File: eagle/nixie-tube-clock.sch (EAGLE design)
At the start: 88 parts, among them IC1 HV5622QC, IC2 HV5622QC, IC3 LM555D, IC5 LD117ADT33TR, P1 1 k, Q1 BC817-25SMD, Q2 BC817-25SMD, Q3 BC817-25SMD, Q4 BC817-25SMD, T1 BC547B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

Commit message: Alfa v2 version of schematic
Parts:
- removed R39, R40, R41, R42: 100 k, resistor:R-EU_R1206
- Q1, Q2, Q3, Q4: value BC817-25SMD -> BSS138; device transistor-npn:BC817-25SMD -> transistor-small-signal:BSS123
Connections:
- removed net N$1: Q1.B, R39.1
- removed net N$17: Q3.B, R41.1
- removed net N$2: Q2.B, R40.1
- removed net N$31: Q4.B, R42.1
- net +12V: now also Q1.D, Q2.D; no longer R37.2, R38.2
- net BL: now also Q4.D; no longer Q4.C
- net CLK: now also Q2.S, R37.2; no longer Q2.C, R37.1
- net GND: now also Q3.S, Q4.S, R37.1, R38.1; no longer Q1.E, Q2.E, Q3.E, Q4.E
- net LE: now also Q3.D; no longer Q3.C
- net MOSI: now also Q1.S, R38.2; no longer Q1.C, R38.1
- net N$19: now also Q4.G; no longer R42.2
- net N$23: now also Q1.G; no longer R39.2
- net N$25: now also Q2.G; no longer R40.2
- net N$29: now also Q3.G; no longer R41.2
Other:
- moved on the sheet: R37, R38

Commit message: Beta version of schematic
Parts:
- removed LSP1: SCL, solpad:SE11
- removed LSP2: MISO, solpad:SE11
- removed LSP3: MOSI, solpad:SE11
- removed LSP4: VCC, solpad:SE11
- removed LSP5: RST, solpad:SE11
- removed Q2, Q3: BSS138, transistor-small-signal:BSS123
- removed R32, R33, R34: 470, resistor:R-EU_R1206
- removed U$1: TINY2313, atmel:TINY2313
- removed X4: (no value), con-ptr500:AK300/2
- added +: +, testpad:TPPAD1-17
- added -: -, testpad:TPPAD1-17
- added C8, C9: 22 pF, resistor:C-EUC1206
- added IC4: MEGA8-AI, atmel:MEGA8-AI
- added MISO: MISO, solpad:SE11
- added MOSI: MOSI, solpad:SE11
- added RST: RST, solpad:SE11
- added SCK: SCK, solpad:SE11
- added T7, T8, T9: IRLL014NTRPBF, transistor-fet:IRLL014NTRPBF
- added VCC: VCC, solpad:SE11
- C1: value 47 uF / 16 V -> 100 uF / 16 V
- D1: value GF1 -> 1A 600V
- Q1: value BSS138 -> 8 MHz; device transistor-small-signal:BSS123 -> crystal:CRYSTALHC49S
- R13, R46: value 270 -> 330k
- R16, R17, R19, R20, R22, R23, R25, R26: value 150 -> 270
- R18, R21, R24, R27: value 180 -> 330
- T3, T4, T5: value BST51 -> BSS138; device transistor:-NPN-SOT89-BCE -> transistor-small-signal:BSS123
- renumbered D2 to D1, Q4 to T6
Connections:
- removed net N$135: R34.2, T5.B
- removed net N$136: R32.2, T3.B
- removed net N$137: R33.2, T4.B
- removed net N$24: LED2-B.C
- removed net N$30: LED3-B.C
- removed net N$35: LSP5.MP, U$1.PA2(RESET/DW)
- removed net N$36: LED4-B.C
- removed net N$37: LSP3.MP, U$1.(MOSI/DI/SDA/PCINT5)PB5
- removed net N$42: LED5-B.C
- removed net N$48: LED6-B.C
- removed net N$54: LED7-B.C
- new net N$1: IC4.PC6(/RESET), RST.MP
- new net N$17: IC4.PB4(MISO), MISO.MP
- new net N$2: IC4.PB3(MOSI/OC2), MOSI.MP, T3.G
- new net N$31: C9.1, IC4.PB6(XTAL1/TOSC1), Q1.1
- net +12V: now also +.TP, T3.D, T4.D; no longer Q1.D, Q2.D, X4-1.KL
- net +3V3: now also IC4.AVCC, IC4.VCC@1, IC4.VCC@2, VCC.MP; no longer LSP4.MP, U$1.VCC
- net CLK: now also T4.S; no longer Q2.S
- net E_RX: now also IC4.PD1(TXD); no longer U$1.(TXD)PD1
- net E_TX: now also IC4.PD0(RXD); no longer U$1.(RXD)PD0
- net GND: now also -.TP, C8.2, C9.2, IC4.GND, IC4.GND@1, IC4.GND@2, T5.S, T7.S, T8.S, T9.S; no longer Q3.S, T3.E, T4.E, T5.E, U$1.GND, X4-2.KL
- net LE: now also T5.D; no longer Q3.D
- net LED_B: now also LED2-B.C, LED3-B.C, LED4-B.C, LED5-B.C, LED6-B.C, LED7-B.C, T7.D; no longer T4.C
- net LED_D0: now also IC4.PC0(ADC0), T9.G; no longer R34.1, U$1.(OC0A/PCINT2)PB2
- net LED_D1: now also IC4.PC1(ADC1), T8.G; no longer R32.1, U$1.(OC1A/PCINT3)PB3
- net LED_D2: now also IC4.PC2(ADC2), T7.G; no longer R33.1, U$1.(OC1B/PCINT4)PB4
- net LED_G: now also T8.D; no longer T3.C
- net LED_R: now also T9.D; no longer T5.C
- net MIN_1_0: now also IC2.HVOUT23; no longer IC2.HVOUT22, IC2.HVOUT32
- net MIN_1_1: now also IC2.HVOUT24; no longer IC2.HVOUT23
- net MIN_1_2: now also IC2.HVOUT25; no longer IC2.HVOUT24
- net MIN_1_3: now also IC2.HVOUT26; no longer IC2.HVOUT25
- net MIN_1_4: now also IC2.HVOUT27; no longer IC2.HVOUT26
- net MIN_1_5: now also IC2.HVOUT28; no longer IC2.HVOUT27
- net MIN_1_6: now also IC2.HVOUT29; no longer IC2.HVOUT28
- net MIN_1_7: now also IC2.HVOUT30; no longer IC2.HVOUT29
- net MIN_1_8: now also IC2.HVOUT31; no longer IC2.HVOUT30
- net MIN_1_9: now also IC2.HVOUT32; no longer IC2.HVOUT31
- net MOSI: now also T3.S; no longer Q1.S
- net N$19: now also IC4.PB1(OC1A); no longer U$1.(ICP)PD6
- net N$23: now also C8.1, IC4.PB7(XTAL2/TOSC2), Q1.2; no longer LSP2.MP, Q1.G, U$1.(MISO/DO/PCINT6)PB6
- net N$25: now also IC4.PB5(SCK), SCK.MP, T4.G; no longer LSP1.MP, Q2.G, U$1.(UCSK/SCL/PCINT7)PB7
- net N$29: now also IC4.PB0(ICP), T5.G; no longer Q3.G, U$1.(OC0B/T1)PD5
- net RST: now also IC4.PD2(INT0); no longer U$1.(T0)PD4
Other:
- moved on the sheet: R37, R38

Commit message: Small update on sch + added PCB
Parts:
- added GL3, GL4: GLIMMLAMP, 00_own:GLIMMLAMP
- added H1, H3, H4: MOUNT-HOLE3.2, holes:MOUNT-HOLE3.2
- added R32, R33: 330k, resistor:R-EU_R1206
- Q1: value 8 MHz -> 7.3728 MHz
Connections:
- new net N$24: GL3.P$1, R32.1
- new net N$30: GL4.P$1, R33.1
- net GLIMM_0: now also GL3.P$2
- net GLIMM_1: now also GL4.P$2
- net V+: now also R32.2, R33.2
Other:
- moved on the sheet: GL2, LED4-B, LED4-G, LED4-R, LED5-B, LED5-G, LED5-R, LED6-B, LED6-G, LED6-R, LED7-B, LED7-G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

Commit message: Pre-release version of PCB
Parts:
- added C10: 100 n, resistor:C-EUC1206
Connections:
- net +3V3: now also C10.1
- net GND: now also C10.2
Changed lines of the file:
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@@
 <part name="R33" library="resistor" deviceset="R-EU_" device="R1206" value="330k"/>
 <part name="P+43" library="supply1" deviceset="V+" device=""/>
+<part name="C10" library="resistor" deviceset="C-EU" device="C1206" value="100 n"/>
+<part name="+3V4" library="supply1" deviceset="+3V3" device=""/>
+<part name="GND18" library="supply1" deviceset="GND" device=""/>
 </parts>
 <sheets>
@@
 <instance part="R33" gate="G$1" x="226.06" y="81.28" rot="R90"/>
 <instance part="P+43" gate="1" x="226.06" y="91.44"/>
+<instance part="C10" gate="G$1" x="-193.04" y="48.26"/>
+<instance part="+3V4" gate="G$1" x="-193.04" y="55.88"/>
+<instance part="GND18" gate="1" x="-193.04" y="38.1"/>
 </instances>
 <busses>
@@
 <junction x="-190.5" y="-7.62"/>
 </segment>
+<segment>
+<pinref part="C10" gate="G$1" pin="2"/>
+<pinref part="GND18" gate="1" pin="GND"/>
+<wire x1="-193.04" y1="43.18" x2="-193.04" y2="40.64" width="0.1524" layer="91"/>
+</segment>
 </net>
 <net name="SEC_1_0" class="0">
@@
 <wire x1="-177.8" y1="-7.62" x2="-175.26" y2="-7.62" width="0.1524" layer="91"/>
 </segment>
-</net>
+<segment>
+<pinref part="+3V4" gate="G$1" pin="+3V3"/>
+<pinref part="C10" gate="G$1" pin="1"/>
+<wire x1="-193.04" y1="53.34" x2="-193.04" y2="50.8" width="0.1524" layer="91"/>
+</segment>
+</net>

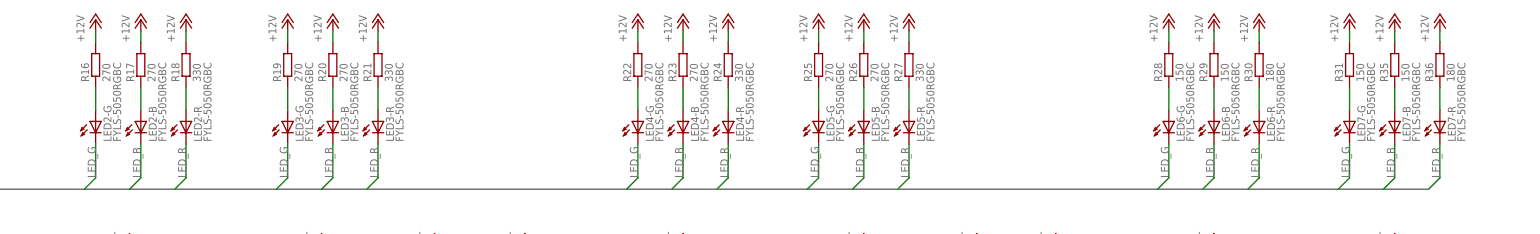
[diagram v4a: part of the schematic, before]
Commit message: Replaced RGB LED + Gerber files
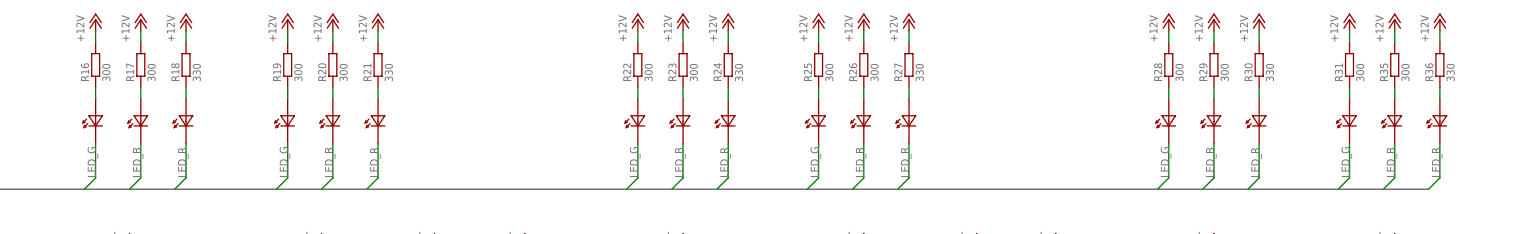
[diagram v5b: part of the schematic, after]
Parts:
- removed LED2, LED3, LED4, LED5, LED6, LED7: FYLS-5050RGBC, 00_own:FYLS-5050RGBC
- added U$1, U$3, U$4, U$5, U$6, U$7: OF-SMD5060RGB, 00_own:OF-SMD5060RGB
- R16, R17, R19, R20, R22, R23, R25, R26: value 270 -> 300
- R28, R29, R31, R35: value 150 -> 300
- R30, R36: value 180 -> 330
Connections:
- net LED_B: now also U$1B.CATH, U$3B.CATH, U$4B.CATH, U$5B.CATH, U$6B.CATH, U$7B.CATH; no longer LED2-B.C, LED3-B.C, LED4-B.C, LED5-B.C, LED6-B.C, LED7-B.C
- net LED_G: now also U$1G.CATH, U$3G.CATH, U$4G.CATH, U$5G.CATH, U$6G.CATH, U$7G.CATH; no longer LED2-G.C, LED3-G.C, LED4-G.C, LED5-G.C, LED6-G.C, LED7-G.C
- net LED_R: now also U$1R.CATH, U$3R.CATH, U$4R.CATH, U$5R.CATH, U$6R.CATH, U$7R.CATH; no longer LED2-R.C, LED3-R.C, LED4-R.C, LED5-R.C, LED6-R.C, LED7-R.C
- net N$20: now also U$1G.ANODE; no longer LED2-G.A
- net N$21: now also U$1B.ANODE; no longer LED2-B.A
- net N$22: now also U$1R.ANODE; no longer LED2-R.A
- net N$26: now also U$3G.ANODE; no longer LED3-G.A
- net N$27: now also U$3B.ANODE; no longer LED3-B.A
- net N$28: now also U$3R.ANODE; no longer LED3-R.A
- net N$32: now also U$4G.ANODE; no longer LED4-G.A
- net N$33: now also U$4B.ANODE; no longer LED4-B.A
- net N$34: now also U$4R.ANODE; no longer LED4-R.A
- net N$38: now also U$5G.ANODE; no longer LED5-G.A
- net N$39: now also U$5B.ANODE; no longer LED5-B.A
- net N$40: now also U$5R.ANODE; no longer LED5-R.A
- net N$44: now also U$6G.ANODE; no longer LED6-G.A
- net N$45: now also U$6B.ANODE; no longer LED6-B.A
- net N$46: now also U$6R.ANODE; no longer LED6-R.A
- net N$50: now also U$7G.ANODE; no longer LED7-G.A
- net N$51: now also U$7B.ANODE; no longer LED7-B.A
- net N$52: now also U$7R.ANODE; no longer LED7-R.A

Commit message: Some reworks around the HV5622 ans ESP
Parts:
- added H2: MOUNT-HOLE3.2, holes:MOUNT-HOLE3.2
- added R34, R39: 10 k, resistor:R-EU_R1206
- added T10: BSS138, transistor-small-signal:BSS123
- L1: value 150 u / 1 A -> 100 u / 1 A
- R14, R15, R37, R38: value 100 k -> 10 k
- R16, R17, R19, R20, R22, R23, R25, R26, R28, R29, R31, R35: value 300 -> 470
- R18, R21, R24, R27, R30, R36: value 330 -> 510
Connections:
- removed net N$1: IC4.PC6(/RESET), RST.MP
- removed net N$25: IC4.PB5(SCK), SCK.MP, T4.G
- new net CH_PD: IC4.PD3(INT1), U$2.CH_PD
- new net N$35: IC4.PB5(SCK), SCK.MP, T3.G
- new net N$41: IC4.PB3(MOSI/OC2), MOSI.MP, T10.G
- new net N$43: IC4.PD7(AIN1), T4.G
- new net POL: IC1.POL, IC2.POL, R37.1, T4.D
- net +12V: now also R34.2, R37.2, R38.2; no longer IC1.POL, IC2.POL, T3.D, T4.D
- net +3V3: now also R39.2; no longer U$2.CH_PD
- net CLK: now also R38.1, T3.D; no longer R37.2, T4.S
- net GND: now also T10.S, T3.S, T4.S; no longer R37.1, R38.1
- net MOSI: now also R34.1, T10.D; no longer R38.2, T3.S
- net N$2: now also IC4.PC6(/RESET), R39.1, RST.MP; no longer IC4.PB3(MOSI/OC2), MOSI.MP, T3.G
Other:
- moved on the sheet: C10, MISO, MOSI, R15, R37, R38, T3, T4, T5, T6

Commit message: Final adjustments
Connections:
- new net GLIMM_2: GL2.P$2, IC2.HVOUT17
- new net GLIMM_3: GL4.P$2, IC2.HVOUT18
- net GLIMM_0: now also IC1.HVOUT7; no longer GL3.P$2, IC1.HVOUT8
- net GLIMM_1: now also GL3.P$2, IC1.HVOUT8; no longer GL2.P$2, GL4.P$2, IC2.HVOUT17
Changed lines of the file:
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@@
 </instances>
 <busses>
-<bus name="SEC_1_[0..9],SEC_10_[0..5],MIN_1_[0..9],MIN_10_[0..5],HOUR_1_[0..9],HOUR_10_[0..2],GLIMM_[0..1]">
+<bus name="SEC_1_[0..9],SEC_10_[0..5],MIN_1_[0..9],MIN_10_[0..5],HOUR_1_[0..9],HOUR_10_[0..2],GLIMM_[0..3]">
 <segment>
 <wire x1="309.88" y1="40.64" x2="157.48" y2="40.64" width="0.762" layer="92"/>
@@
 </segment>
 <segment>
-<wire x1="76.2" y1="-30.48" x2="73.66" y2="-33.02" width="0.1524" layer="91"/>
-<pinref part="IC1" gate="G$1" pin="HVOUT8"/>
-<wire x1="73.66" y1="-33.02" x2="55.88" y2="-33.02" width="0.1524" layer="91"/>
-<label x="58.42" y="-33.02" size="1.778" layer="95"/>
-</segment>
-<segment>
-<wire x1="104.14" y1="40.64" x2="106.68" y2="43.18" width="0.1524" layer="91"/>
-<pinref part="GL3" gate="GL" pin="P$2"/>
-<wire x1="106.68" y1="43.18" x2="106.68" y2="58.42" width="0.1524" layer="91"/>
-<label x="106.68" y="43.18" size="1.778" layer="95" rot="R90"/>
-</segment>
-</net>
-<net name="GLIMM_1" class="0">
-<segment>
-<wire x1="205.74" y1="40.64" x2="208.28" y2="43.18" width="0.1524" layer="91"/>
-<pinref part="GL2" gate="GL" pin="P$2"/>
-<wire x1="208.28" y1="43.18" x2="208.28" y2="58.42" width="0.1524" layer="91"/>
-<label x="208.28" y="43.18" size="1.778" layer="95" rot="R90"/>
-</segment>
-<segment>
-<wire x1="157.48" y1="-7.62" x2="154.94" y2="-10.16" width="0.1524" layer="91"/>
-<pinref part="IC2" gate="G$1" pin="HVOUT17"/>
-<wire x1="154.94" y1="-10.16" x2="142.24" y2="-10.16" width="0.1524" layer="91"/>
-<label x="144.78" y="-10.16" size="1.778" layer="95"/>
-</segment>
-<segment>
-<wire x1="223.52" y1="40.64" x2="226.06" y2="43.18" width="0.1524" layer="91"/>
-<pinref part="GL4" gate="GL" pin="P$2"/>
-<wire x1="226.06" y1="43.18" x2="226.06" y2="58.42" width="0.1524" layer="91"/>
-<label x="226.06" y="43.18" size="1.778" layer="95" rot="R90"/>
+<wire x1="76.2" y1="-33.02" x2="73.66" y2="-35.56" width="0.1524" layer="91"/>
+<pinref part="IC1" gate="G$1" pin="HVOUT7"/>
+<wire x1="73.66" y1="-35.56" x2="55.88" y2="-35.56" width="0.1524" layer="91"/>
+<label x="58.42" y="-35.56" size="1.778" layer="95"/>
 </segment>
 </net>
@@
 </segment>
 </net>
+<net name="GLIMM_1" class="0">
+<segment>
+<wire x1="104.14" y1="40.64" x2="106.68" y2="43.18" width="0.1524" layer="91"/>
+<pinref part="GL3" gate="GL" pin="P$2"/>
+<wire x1="106.68" y1="43.18" x2="106.68" y2="58.42" width="0.1524" layer="91"/>
+<label x="106.68" y="43.18" size="1.778" layer="95" rot="R90"/>
+</segment>
+<segment>
+<wire x1="76.2" y1="-30.48" x2="73.66" y2="-33.02" width="0.1524" layer="91"/>
+<pinref part="IC1" gate="G$1" pin="HVOUT8"/>
+<wire x1="73.66" y1="-33.02" x2="55.88" y2="-33.02" width="0.1524" layer="91"/>
+<label x="58.42" y="-33.02" size="1.778" layer="95"/>
+</segment>
+</net>
+<net name="GLIMM_2" class="0">
+<segment>
+<wire x1="205.74" y1="40.64" x2="208.28" y2="43.18" width="0.1524" layer="91"/>
+<pinref part="GL2" gate="GL" pin="P$2"/>
+<wire x1="208.28" y1="43.18" x2="208.28" y2="58.42" width="0.1524" layer="91"/>
+<label x="208.28" y="43.18" size="1.778" layer="95" rot="R90"/>
+</segment>
+<segment>
+<wire x1="157.48" y1="-7.62" x2="154.94" y2="-10.16" width="0.1524" layer="91"/>
+<pinref part="IC2" gate="G$1" pin="HVOUT17"/>
+<wire x1="154.94" y1="-10.16" x2="142.24" y2="-10.16" width="0.1524" layer="91"/>
+<label x="144.78" y="-10.16" size="1.778" layer="95"/>
+</segment>
+</net>
+<net name="GLIMM_3" class="0">
+<segment>
+<wire x1="223.52" y1="40.64" x2="226.06" y2="43.18" width="0.1524" layer="91"/>
+<pinref part="GL4" gate="GL" pin="P$2"/>
+<wire x1="226.06" y1="43.18" x2="226.06" y2="58.42" width="0.1524" layer="91"/>
+<label x="226.06" y="43.18" size="1.778" layer="95" rot="R90"/>
+</segment>
+<segment>
+<wire x1="157.48" y1="-5.08" x2="154.94" y2="-7.62" width="0.1524" layer="91"/>
+<pinref part="IC2" gate="G$1" pin="HVOUT18"/>
+<wire x1="154.94" y1="-7.62" x2="142.24" y2="-7.62" width="0.1524" layer="91"/>
+<label x="144.78" y="-7.62" size="1.778" layer="95"/>
+</segment>
+</net>
